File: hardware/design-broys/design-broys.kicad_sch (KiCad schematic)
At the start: 0 parts

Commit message: Added esp32
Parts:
- added U1: ESP32-C3FH4, QFN50P500X500X90-33N, symbol ESP32-C3FH4:ESP32-C3FH4
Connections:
- new net: U1.2 (VDD3P3), U1.3 (VDD3P3)
- new net: U1.31 (VDDA), U1.32 (VDDA)
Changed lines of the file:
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@@
     (company "lilordag")
+  )
+  (symbol (lib_id "ESP32-C3FH4:ESP32-C3FH4") (at 64.77 72.39 0) (unit 1)
+    (in_bom yes) (on_board yes) (fields_autoplaced)
+    (property "Reference" "U1" (id 0) (at 64.77 34.29 0))
+    (property "Value" "ESP32-C3FH4" (id 1) (at 64.77 36.83 0))
+    (property "Footprint" "QFN50P500X500X90-33N" (id 2) (at 64.77 72.39 0)
+      (effects (font (size 1.27 1.27)) (justify left bottom) hide)
+    )
+    (property "Datasheet" "" (id 3) (at 64.77 72.39 0)
+      (effects (font (size 1.27 1.27)) (justify left bottom) hide)
+    )
+    (property "MANUFACTURER" "Espressif" (id 4) (at 64.77 72.39 0)
+      (effects (font (size 1.27 1.27)) (justify left bottom) hide)
+    )
+    (property "PARTREV" "V1.0" (id 5) (at 64.77 72.39 0)
+      (effects (font (size 1.27 1.27)) (justify left bottom) hide)
+    )
+    (property "STANDARD" "IPC 7351B" (id 6) (at 64.77 72.39 0)
+      (effects (font (size 1.27 1.27)) (justify left bottom) hide)
+    )
+    (property "MAXIMUM_PACKAGE_HEIGHT" "0.9mm" (id 7) (at 64.77 72.39 0)
+      (effects (font (size 1.27 1.27)) (justify left bottom) hide)
+    )
+    (pin "1")
+    (pin "10")
+    (pin "11")
+    (pin "12")
+    (pin "13")
+    (pin "14")
+    (pin "15")
+    (pin "16")
+    (pin "17")
+    (pin "18")
+    (pin "19")
+    (pin "2")
+    (pin "20")
+    (pin "21")
+    (pin "22")
+    (pin "23")
+    (pin "24")
+    (pin "25")
+    (pin "26")
+    (pin "27")
+    (pin "28")
+    (pin "29")
+    (pin "3")
+    (pin "30")
+    (pin "31")
+    (pin "32")
+    (pin "33")
+    (pin "4")
+    (pin "5")
+    (pin "6")
+    (pin "7")
+    (pin "8")
+    (pin "9")
   )
   (sheet_instances
     (path "/" (page "1"))
   )
+  (symbol_instances
+    (path "/f13a47f9-e1fe-4deb-a864-14ed517f891d"
+      (reference "U1") (unit 1) (value "ESP32-C3FH4") (footprint "QFN50P500X500X90-33N")
+    )
+  )
 )

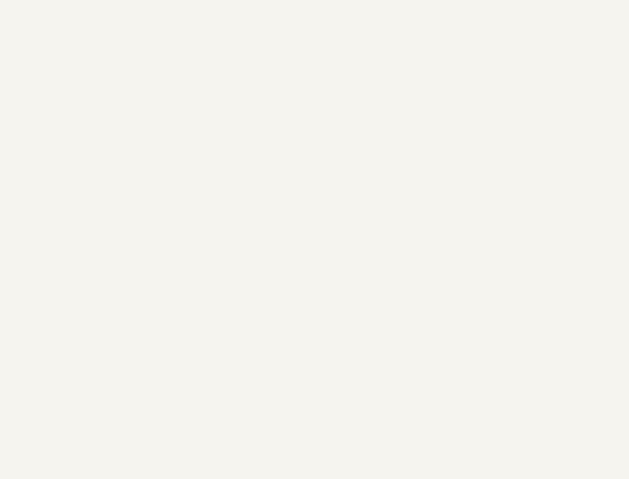
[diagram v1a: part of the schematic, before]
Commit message: Added external 16MBit flash
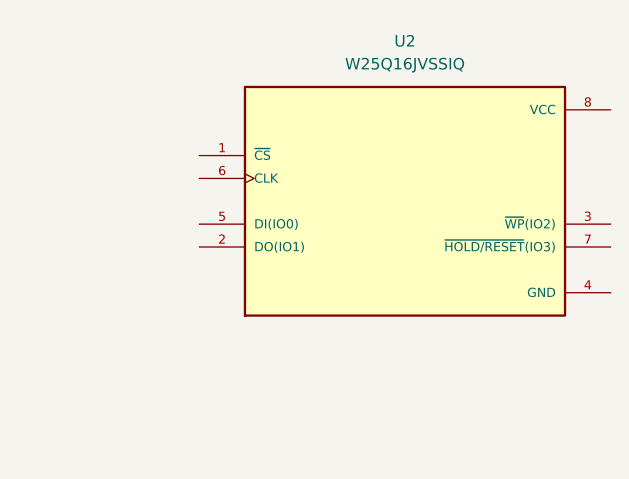
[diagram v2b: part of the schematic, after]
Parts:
- added U2: W25Q16JVSSIQ, W25Q16JVSSIQ:SOIC127P790X216-8N, symbol W25Q16JVSSIQ:W25Q16JVSSIQ
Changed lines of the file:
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@@
     (company "lilordag")
+  )
+  (symbol (lib_id "W25Q16JVSSIQ:W25Q16JVSSIQ") (at 140.97 53.34 0) (unit 1)
+    (in_bom yes) (on_board yes) (fields_autoplaced)
+    (property "Reference" "U2" (id 0) (at 140.97 35.56 0))
+    (property "Value" "W25Q16JVSSIQ" (id 1) (at 140.97 38.1 0))
+    (property "Footprint" "W25Q16JVSSIQ:SOIC127P790X216-8N" (id 2) (at 140.97 53.34 0)
+      (effects (font (size 1.27 1.27)) (justify left bottom) hide)
+    )
+    (property "Datasheet" "" (id 3) (at 140.97 53.34 0)
+      (effects (font (size 1.27 1.27)) (justify left bottom) hide)
+    )
+    (property "PRICE" "None" (id 4) (at 140.97 53.34 0)
+      (effects (font (size 1.27 1.27)) (justify left bottom) hide)
+    )
+    (property "AVAILABILITY" "Unavailable" (id 5) (at 140.97 53.34 0)
+      (effects (font (size 1.27 1.27)) (justify left bottom) hide)
+    )
+    (property "MP" "W25Q16JVSSIQ" (id 6) (at 140.97 53.34 0)
+      (effects (font (size 1.27 1.27)) (justify left bottom) hide)
+    )
+    (property "PACKAGE" "SOIC-8 Winbond" (id 7) (at 140.97 53.34 0)
+      (effects (font (size 1.27 1.27)) (justify left bottom) hide)
+    )
+    (property "DESCRIPTION" "3v 16m-Bit Serial Flash Memory With Dual" (id 8) (at 140.97 53.34 0)
+      (effects (font (size 1.27 1.27)) (justify left bottom) hide)
+    )
+    (property "MF" "Winbond Electronics" (id 9) (at 140.97 53.34 0)
+      (effects (font (size 1.27 1.27)) (justify left bottom) hide)
+    )
+    (pin "1")
+    (pin "2")
+    (pin "3")
+    (pin "4")
+    (pin "5")
+    (pin "6")
+    (pin "7")
+    (pin "8")
   )
   (symbol (lib_id "ESP32-C3FH4:ESP32-C3FH4") (at 64.77 72.39 0) (unit 1)
@@
       (reference "U1") (unit 1) (value "ESP32-C3FH4") (footprint "QFN50P500X500X90-33N")
     )
+    (path "/cd5ad33b-1e02-4f55-b267-df7f2bbfff29"
+      (reference "U2") (unit 1) (value "W25Q16JVSSIQ") (footprint "W25Q16JVSSIQ:SOIC127P790X216-8N")
+    )
   )
